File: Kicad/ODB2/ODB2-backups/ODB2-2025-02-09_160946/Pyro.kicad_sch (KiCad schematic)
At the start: 29 parts, among them U2 TLV2371DBV, U3 74LV1T87GVH

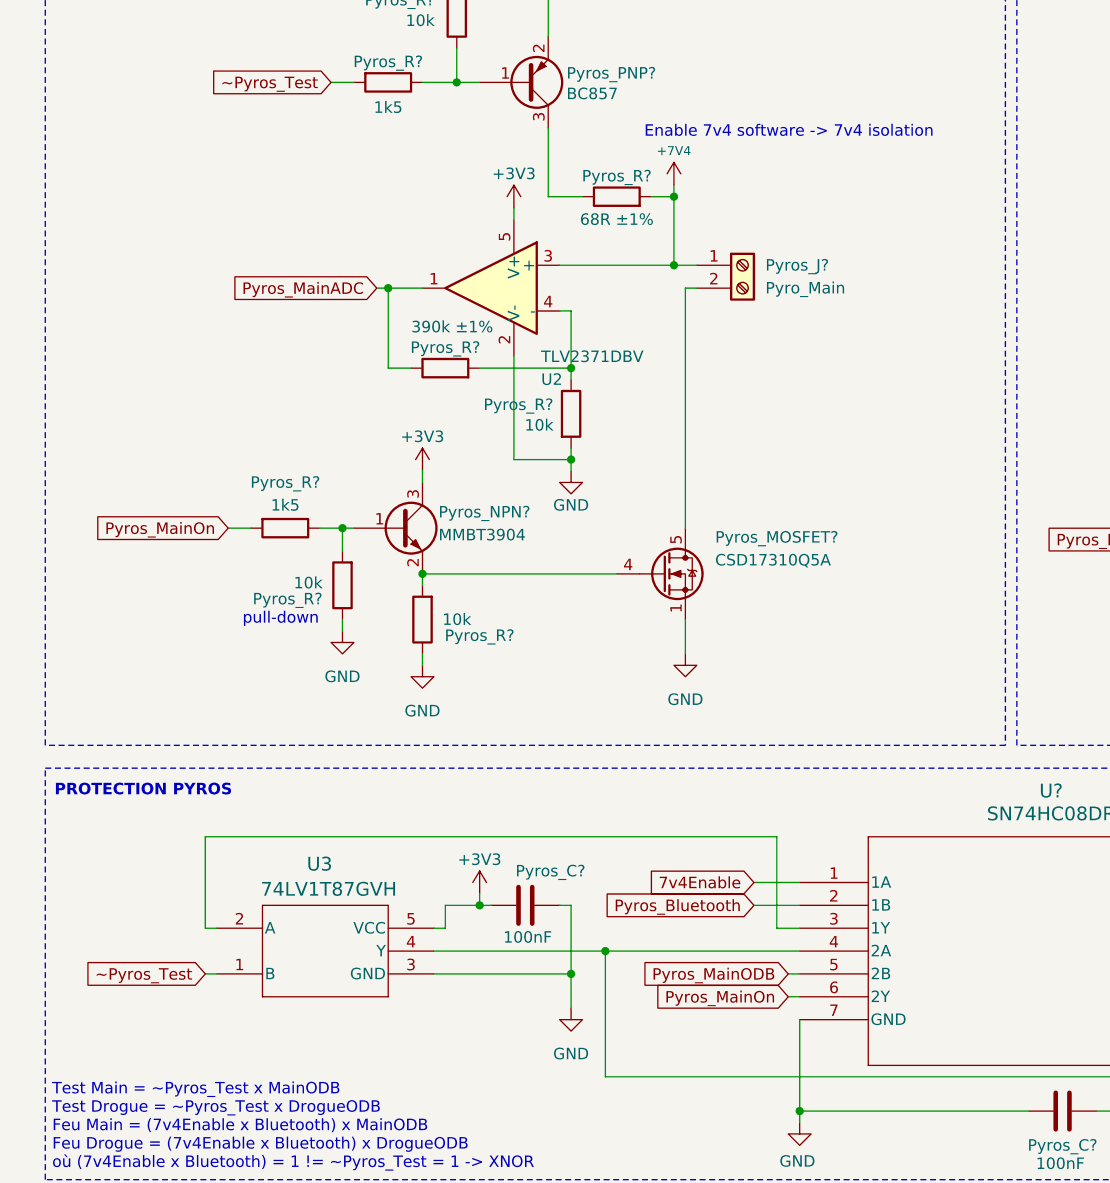
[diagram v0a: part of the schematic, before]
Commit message: Changed XNOR Gate and OP AMP to 1 chanel
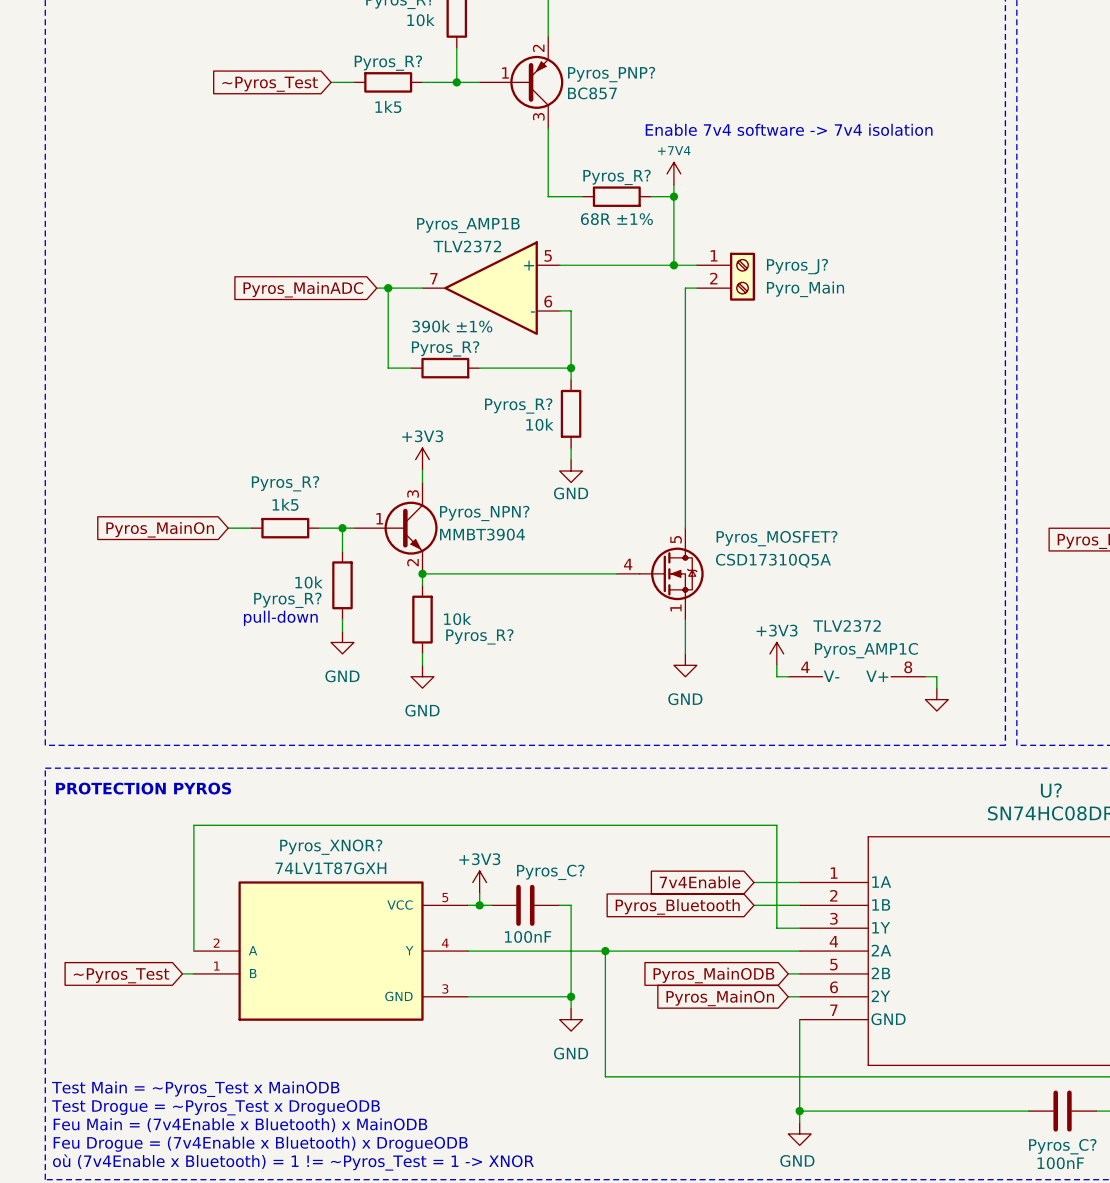
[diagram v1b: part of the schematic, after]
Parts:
- removed U2: TLV2371DBV, Package_TO_SOT_SMD:SOT-23-5, symbol Amplifier_Operational:TLV2371DBV
- removed U3: 74LV1T87GVH, ODB:SC-74A_SOT753_NEX, symbol ODB2:74LV1T87GVH
- added Pyros_AMP1: TLV2372, Package_SO:SOIC-8-1EP_3.9x4.9mm_P1.27mm_EP2.41x3.81mm, symbol Amplifier_Operational:TLV2372
- added Pyros_XNOR?: 74LV1T87GXH, Library:IC_74LV1T87GXH, symbol ODB_Lib:74LV1T87GXH
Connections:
- net +3V3: now also Pyros_AMP1.4 (V-), Pyros_XNOR?.5 (VCC)
- net +7V4: now also Pyros_AMP1.5 (+)
- net GND: now also Pyros_AMP1.8 (V+), Pyros_XNOR?.3 (GND)
- net Pyros_MainADC: now also Pyros_AMP1.7
- net ~Pyros_Test: now also Pyros_XNOR?.1 (B)
- net at Pyros_R?.1, Pyros_R?.2: now also Pyros_AMP1.6 (-)
- net at U?.10 (3B), U?.4 (2A): now also Pyros_XNOR?.4 (Y)
- net at U?.3 (1Y): now also Pyros_XNOR?.2 (A)
